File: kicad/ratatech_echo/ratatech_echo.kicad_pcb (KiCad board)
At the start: 2 copper layers, 99.8 x 90 mm, 108 parts, among them J1 AudioJack2, J2 Conn_01x02, J3 Conn_01x02, J4 AudioJack2, J5 Barrel_Jack_Switch, Q1 2N3904, Q2 2N3906, Q3 2N3904, Q4 2N3906, SW1 SW_SPDT, SW2 SW_SPST, U1 NE5532, U2 NE5532, U3 PT2399, U4 LT1054xSOIC16, U5 LM7812_TO220, U6 LM7912_TO220

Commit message: Routing full done first try
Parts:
- removed C20: 560uF, Capacitor_SMD:C_0603_1608Metric
- added D9: LED, LED_SMD:LED_1206_3216Metric, F.Cu at (106.7, 86.2)
- added G***: LOGO, imgs:ratatech_bitmap, F.Cu at (150.7, 78.3)
- added R39: 470, Resistor_SMD:R_0603_1608Metric, F.Cu at (105.5, 105.9)
- added REF**: MountingHole_3mm, MountingHole:MountingHole_3mm, F.Cu at (101.1, 27.0)
- added REF**: MountingHole_3mm, MountingHole:MountingHole_3mm, F.Cu at (101.1, 110.0)
- added REF**: MountingHole_3mm, MountingHole:MountingHole_3mm, F.Cu at (194.0, 26.9)
- added REF**: MountingHole_3mm, MountingHole:MountingHole_3mm, F.Cu at (193.8, 109.9)
- SW1: value SW_SPDT -> SW_DPDT_x2; footprint Connector:FanPinHeader_1x03_P2.54mm_Vertical -> M2028B2B1W03:M2028B2B1W03
- moved D4 93.4 mm to (184.8, 93.8)
- moved C13 25.4 mm to (129.0, 108.3), turned to 0 degrees
- moved RV4 24.7 mm to (159.0, 92.0)
- moved RV3 24.3 mm to (133.6, 92.0)
- moved C12 21.2 mm to (120.3, 108.3)
- moved R33 20.2 mm to (171.9, 55.9), turned to 180 degrees
- moved C35 18.6 mm to (134.7, 45.5)
- moved C33 17.6 mm to (116.3, 46.2)
- moved D8 15.1 mm to (103.9, 50.5)
- moved C29 14.0 mm to (137.7, 108.3)
- moved R31 13.4 mm to (124.9, 47.0), turned to 0 degrees
- moved SW1 12.8 mm to (106.8, 95.7)
- moved Q3 12.4 mm to (156.6, 51.5)
- moved D3 10.7 mm to (167.2, 55.5)
- moved R30 10.3 mm to (114.0, 110.6)
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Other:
- board text added: "Delay level pot"
- board text added: "Delay time pot"
- board text added: "Effect On/Off"
- board text added: "Input clipping"
- board text added: "Input gain pot"
- board text added: "Power ON/OFF"
- board text added: "Ratat-Echo 1.0"
- board text added: "Ratatech 2020"
- board text added: "Reverb dry/wet pot"
- board text added: "Reverb level pot"
- board text added: "Spring reverb in"
- board text added: "Spring reverb out"

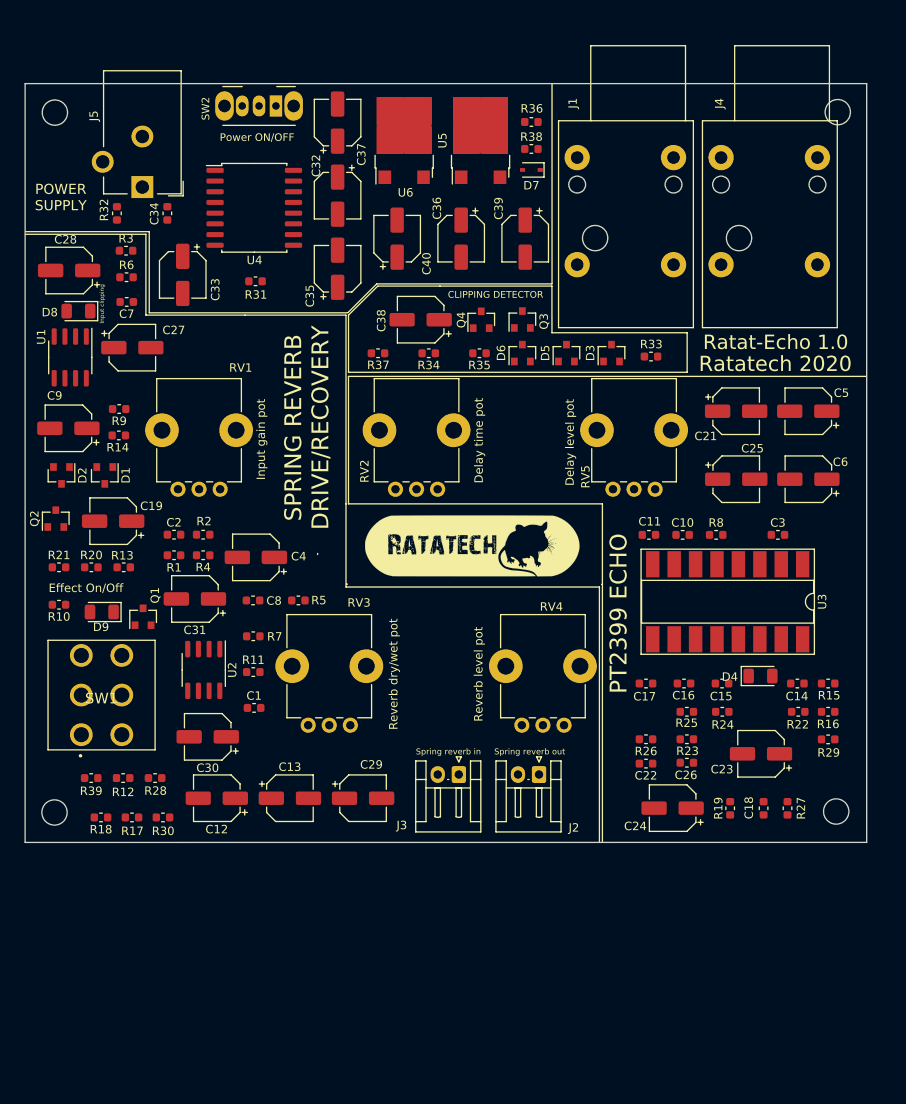
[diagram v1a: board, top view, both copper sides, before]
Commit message: Component rearrengement
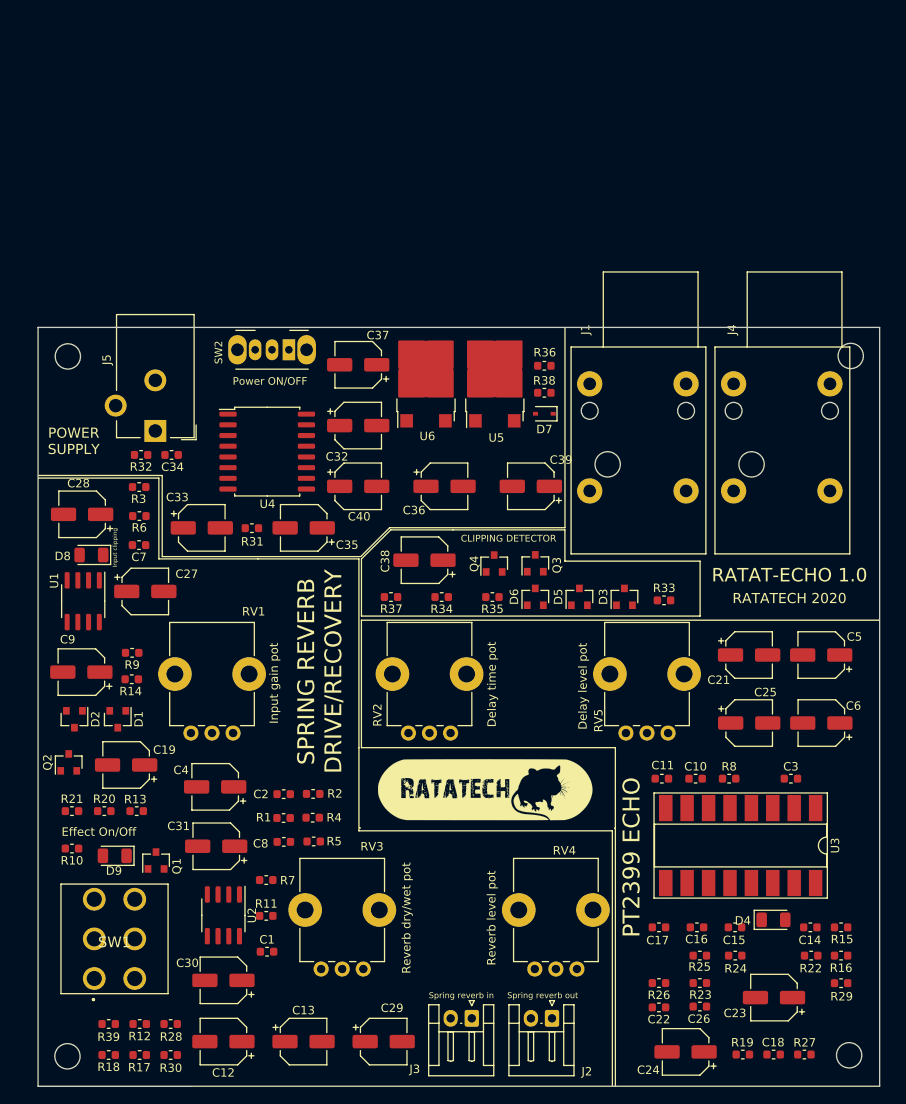
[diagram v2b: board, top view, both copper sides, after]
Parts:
- moved R1 33.8 mm to (128.3, 110.6)
- moved R4 33.7 mm to (131.7, 110.6)
- moved C2 33.4 mm to (128.3, 107.8)
- moved R2 33.4 mm to (131.8, 107.8)
- moved C35 31.0 mm to (130.7, 76.2), turned to 180 degrees
- moved C33 30.1 mm to (118.6, 76.2), turned to 0 degrees
- moved C40 29.7 mm to (137.1, 71.3), turned to 0 degrees
- moved C31 29.4 mm to (120.3, 114.0)
- moved C36 29.4 mm to (147.4, 71.3), turned to 0 degrees
- moved C39 29.4 mm to (157.6, 71.3), turned to 180 degrees
- moved R31 29.3 mm to (124.5, 76.3)
- moved R27 29.3 mm to (190.0, 138.7), turned to 180 degrees
- moved R19 29.2 mm to (182.7, 138.7), turned to 0 degrees
- moved R39 29.2 mm to (107.5, 135.1)
- moved R12 29.2 mm to (111.2, 135.1)
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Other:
- board text added: "RATAT-ECHO 1.0"
- board text added: "RATATECH 2020"
- board text removed: "Ratat-Echo 1.0"
- board text removed: "Ratatech 2020"

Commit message: Autorouting done
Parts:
- removed G***: LOGO, imgs:ratatech_bitmap
- removed REF** (x4): MountingHole_3mm, MountingHole:MountingHole_3mm
- added H1: MountingHole, MountingHole:MountingHole_3mm, F.Cu at (102.6, 55.7)
- added H2: MountingHole, MountingHole:MountingHole_3mm, F.Cu at (195.6, 55.8)
- added H3: MountingHole, MountingHole:MountingHole_3mm, F.Cu at (195.6, 139.1)
- added H4: MountingHole, MountingHole:MountingHole_3mm, F.Cu at (102.4, 139.1)
- added U7: logo, imgs:ratatech_bitmap, F.Cu at (152.6, 107.2)
- moved Q2 0.53 mm to (103.3, 104.0)
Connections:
- Q2 pad 1: VDD -> Net-(Q2-Pad1)
- Q2 pad 3: Net-(Q2-Pad3) -> VDD
- R21 pad 1: Net-(Q2-Pad3) -> Net-(Q2-Pad1)
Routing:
- net GND: track 0.00 -> 549.5 mm, vias 0 -> 1
- net VCC: track 0.00 -> 181.8 mm
- net input: track 0.00 -> 160.4 mm, vias 0 -> 2
- net output: track 0.00 -> 132.1 mm, vias 0 -> 1
- net VDD: track 0.00 -> 127.4 mm, vias 0 -> 5
- net Net-(D4-Pad2): track 0.00 -> 120.9 mm
- net reverb_in-: track 0.00 -> 100.9 mm, vias 0 -> 1
- net Net-(J4-PadT): track 0.00 -> 100.1 mm
- net Net-(C34-Pad1): track 0.00 -> 95.9 mm
- net scaled_input: track 0.00 -> 88.6 mm, vias 0 -> 1
- net reverb_input: track 0.00 -> 84.3 mm
- net reverb_in+: track 0.00 -> 81.6 mm
- net VCC5: track 0.00 -> 72.4 mm
- net Net-(R17-Pad2): track 0.00 -> 71.4 mm
- net Net-(C12-Pad1): track 0.00 -> 67.6 mm, vias 0 -> 2
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- added copper zone on B.Cu, net GND
- added copper zone on F.Cu, net GND
